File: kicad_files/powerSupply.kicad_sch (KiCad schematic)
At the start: 6 parts, among them U5 TPS61088RHLR

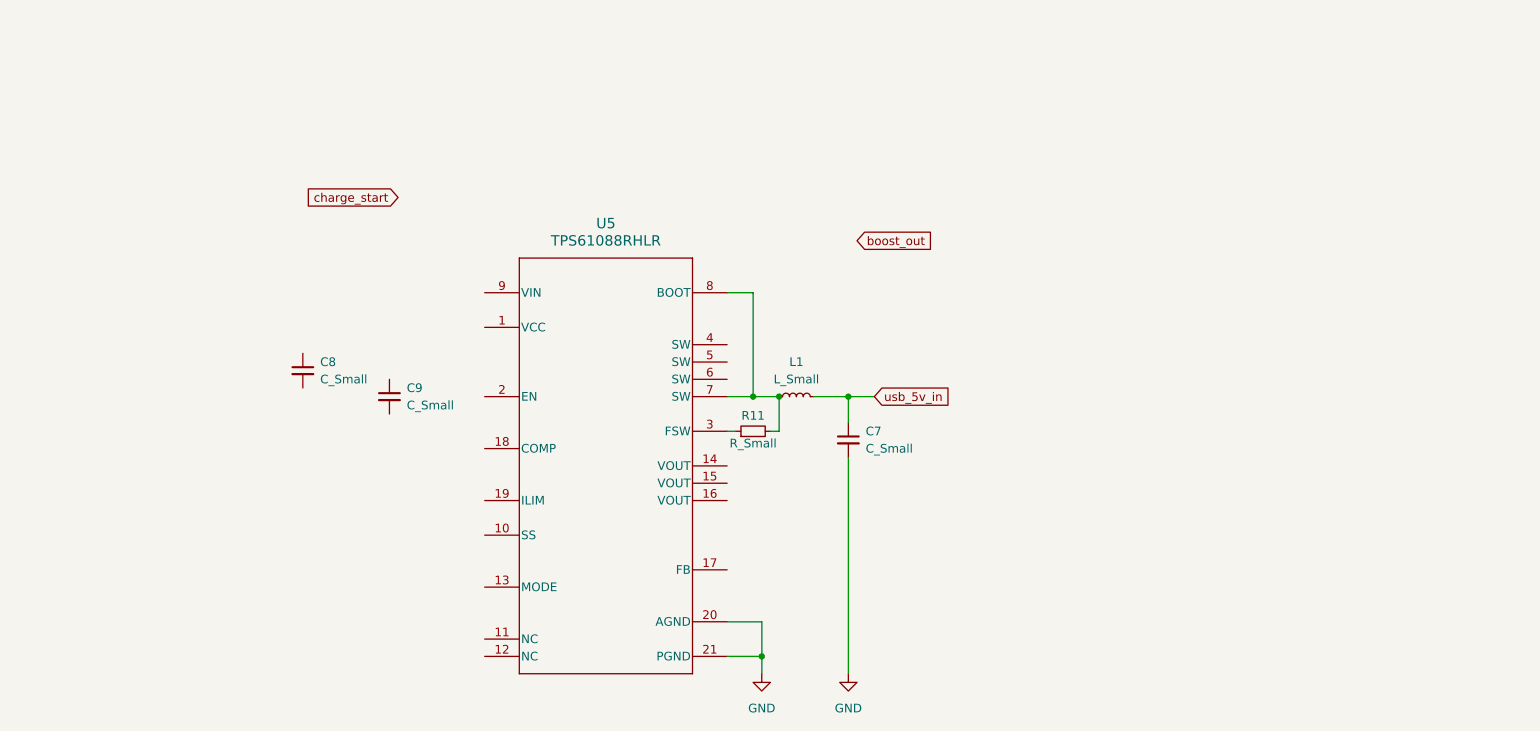
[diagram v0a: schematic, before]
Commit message: finished TI power chip schematic (no values)
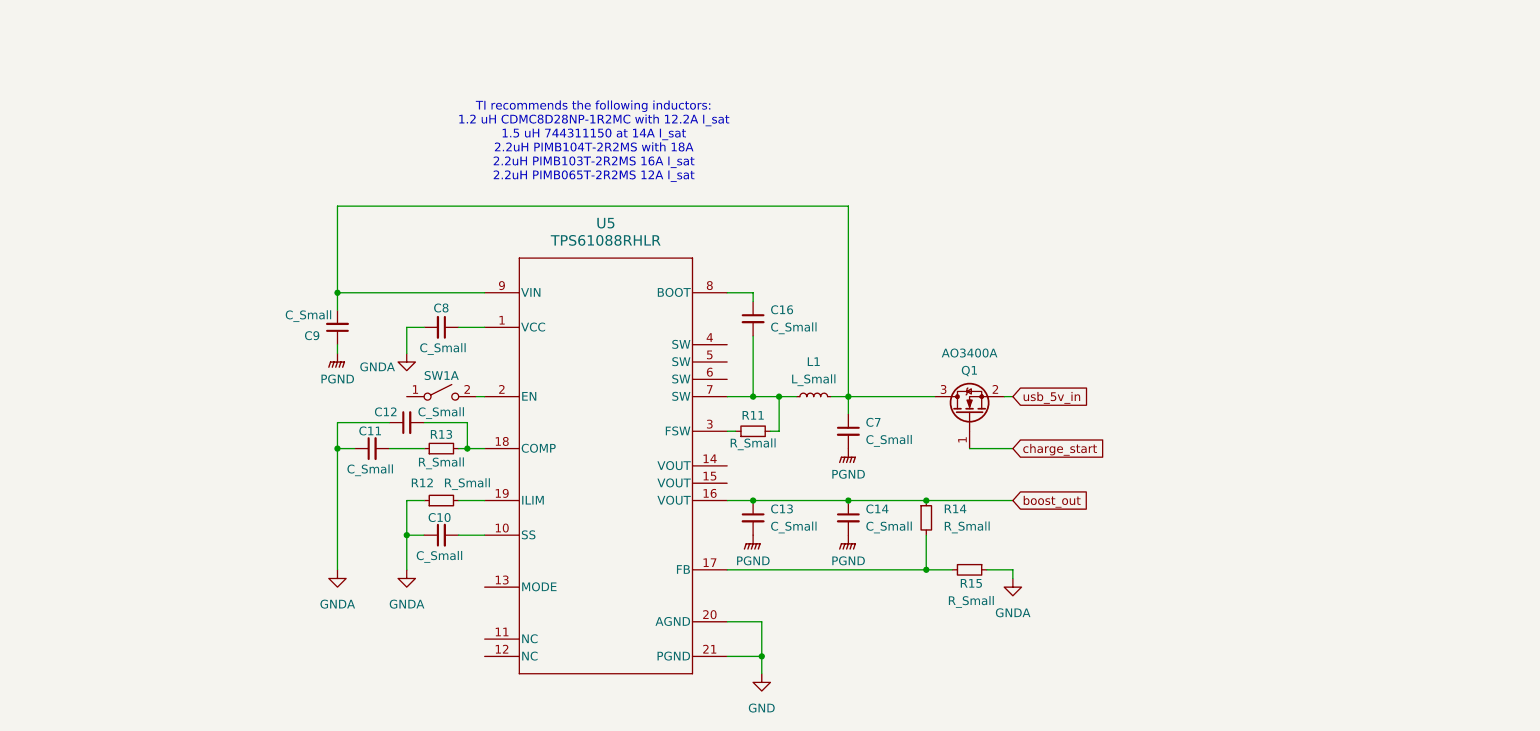
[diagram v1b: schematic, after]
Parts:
- added C10, C11, C12, C13, C14, C16: C_Small, symbol Device:C_Small
- added Q1: AO3400A, Package_TO_SOT_SMD:SOT-23, symbol Transistor_FET:AO3400A
- added R12, R13, R14, R15: R_Small, symbol Device:R_Small
- added SW1: SW_DPST_x2, symbol Switch:SW_DPST_x2
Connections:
- net GND: no longer C7.2
- net boost_out: now also U5.16 (VOUT), C13.1, C14.1, R14.1
- net charge_start: now also Q1.1 (G)
- net usb_5v_in: now also Q1.2 (S); no longer C7.1, L1.2
- net at L1.1, R11.2, U5.7 (SW): now also C16.2; no longer U5.8 (BOOT)
- net PGND: now reaches C9.1
- net PGND: now also C7.2, C13.2, C14.2
- net at C9.2: now also C7.1, L1.2, U5.9 (VIN), Q1.3 (D)
- net at C8.1: now also U5.1 (VCC)
- net GNDA: now reaches C8.2
- net GNDA: now also C10.1, C11.1, C12.1, R12.1, R15.1
- net at U5.10 (SS): now also C10.2
- net at U5.17 (FB): now also R14.2, R15.2
- net at U5.18 (COMP): now also C12.2, R13.2
- net at U5.19 (ILIM): now also R12.2
- net at U5.2 (EN): now also SW1.2 (B)
- new net: C11.2, R13.1
- new net: C16.1, U5.8 (BOOT)
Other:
- note added: "TI recommends the following inductors: 1.2 uH CDMC8D28NP-1R2MC with 12.2A I_sat 1.5 uH 744311150 at 14A I_sat 2.2uH PIMB104T-2R2MS with 18A 2.2uH PIMB103T-2R2MS 16A I_sat 2.2uH PIMB065T-2R2MS 12A I_sat"
- moved on the sheet: C7, C8, C9, L1

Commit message: added symbols for TPS and INA2, sim values for TPS
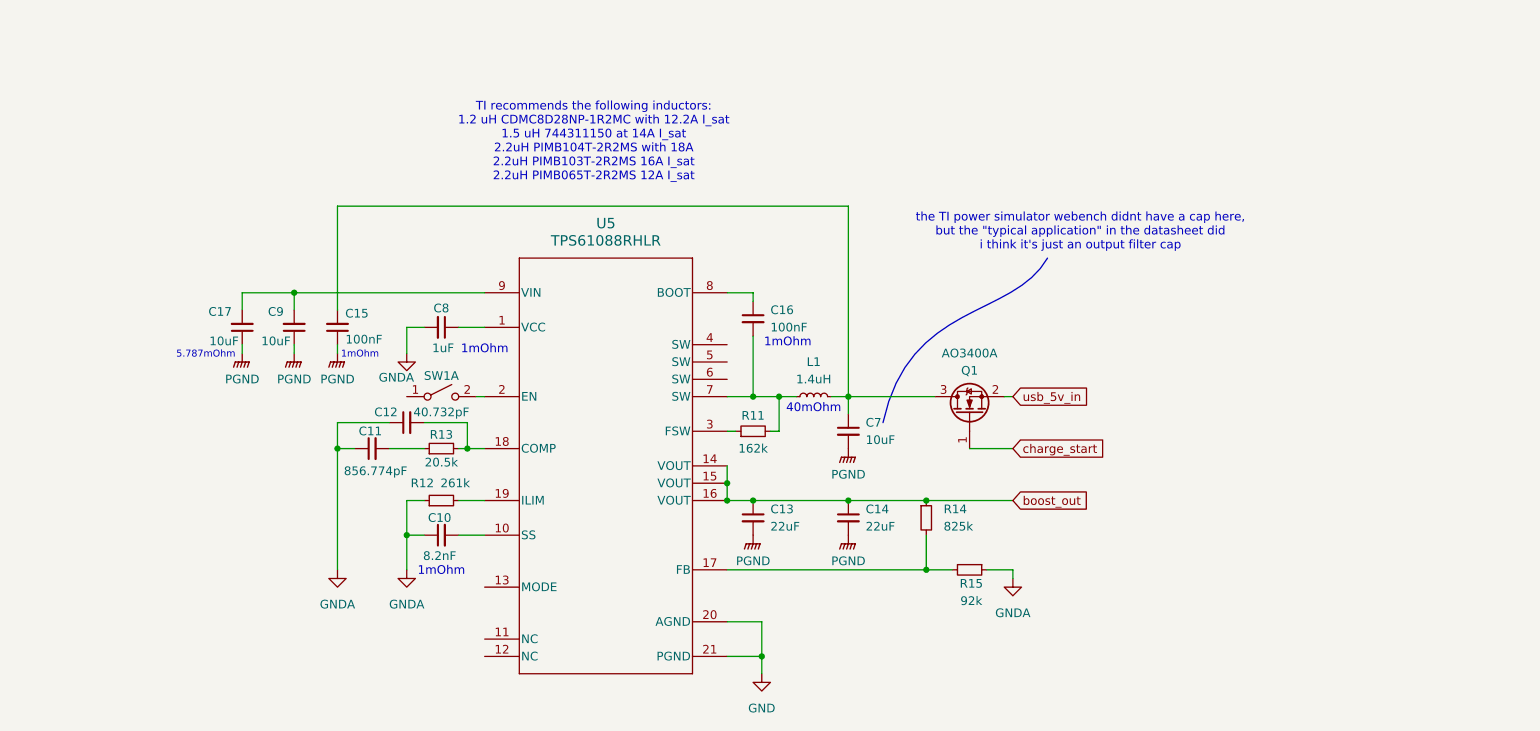
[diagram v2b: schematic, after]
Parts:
- added C15: 100nF, symbol Device:C_Small
- added C17: 10uF, symbol Device:C_Small
- C10: value C_Small -> 8.2nF
- C11: value C_Small -> 856.774pF
- C12: value C_Small -> 40.732pF
- C13, C14: value C_Small -> 22uF
- C16: value C_Small -> 100nF
- C7, C9: value C_Small -> 10uF
- C8: value C_Small -> 1uF
- L1: value L_Small -> 1.4uH
- R11: value R_Small -> 162k
- R12: value R_Small -> 261k
- R13: value R_Small -> 20.5k
- R14: value R_Small -> 825k
- R15: value R_Small -> 92k
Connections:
- net PGND: now also C15.1, C17.1
- net boost_out: now also U5.14 (VOUT), U5.15 (VOUT)
- net at C7.1, L1.2, Q1.3 (D): now also C15.2; no longer C9.2, U5.9 (VIN)
- new net: C17.2, C9.2, U5.9 (VIN)
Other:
- note added: "1mOhm"
- note added: "40mOhm"
- note added: "5.787mOhm"
- note added: "the TI power simulator webench didnt have a cap here, but the "typical application" in the datasheet did i think it's just an output filter cap"
- moved on the sheet: C9

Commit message: more laying out
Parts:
- C10, C11, C12, C13, C14, C15, C16, C17, C7, C8, C9: footprint (none) -> Capacitor_SMD:C_0805_2012Metric_Pad1.18x1.45mm_HandSolder
- L1: footprint (none) -> Inductor_SMD:L_0201_0603Metric
- R11, R12, R13, R14, R15: footprint (none) -> Resistor_SMD:R_0805_2012Metric_Pad1.20x1.40mm_HandSolder
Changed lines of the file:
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@@
 			)
 		)
-		(property "Footprint" ""
+		(property "Footprint" "Capacitor_SMD:C_0805_2012Metric_Pad1.18x1.45mm_HandSolder"
 			(at 127 93.98 0)
 			(hide yes)
@@
 			)
 		)
-		(property "Footprint" ""
+		(property "Footprint" "Capacitor_SMD:C_0805_2012Metric_Pad1.18x1.45mm_HandSolder"
 			(at 172.72 91.44 0)
 			(hide yes)
@@
 			)
 		)
-		(property "Footprint" ""
+		(property "Footprint" "Capacitor_SMD:C_0805_2012Metric_Pad1.18x1.45mm_HandSolder"
 			(at 121.92 77.47 0)
 			(hide yes)
@@
 			)
 		)
-		(property "Footprint" ""
+		(property "Footprint" "Resistor_SMD:R_0805_2012Metric_Pad1.20x1.40mm_HandSolder"
 			(at 204.47 99.06 0)
 			(hide yes)
@@
 			)
 		)
-		(property "Footprint" ""
+		(property "Footprint" "Inductor_SMD:L_0201_0603Metric"
 			(at 181.61 73.66 0)
 			(hide yes)
@@
 			)
 		)
-		(property "Footprint" ""
+		(property "Footprint" "Capacitor_SMD:C_0805_2012Metric_Pad1.18x1.45mm_HandSolder"
 			(at 97.79 63.5 0)
 			(hide yes)
@@
 			)
 		)
-		(property "Footprint" ""
+		(property "Footprint" "Capacitor_SMD:C_0805_2012Metric_Pad1.18x1.45mm_HandSolder"
 			(at 116.84 81.28 0)
 			(hide yes)
@@
 			)
 		)
-		(property "Footprint" ""
+		(property "Footprint" "Capacitor_SMD:C_0805_2012Metric_Pad1.18x1.45mm_HandSolder"
 			(at 105.41 63.5 0)
 			(hide yes)
@@
 			)
 		)
-		(property "Footprint" ""
+		(property "Footprint" "Resistor_SMD:R_0805_2012Metric_Pad1.20x1.40mm_HandSolder"
 			(at 198.12 91.44 0)
 			(hide yes)
@@
 			)
 		)
-		(property "Footprint" ""
+		(property "Footprint" "Resistor_SMD:R_0805_2012Metric_Pad1.20x1.40mm_HandSolder"
 			(at 127 81.28 0)
 			(hide yes)
@@
 			)
 		)
-		(property "Footprint" ""
+		(property "Footprint" "Resistor_SMD:R_0805_2012Metric_Pad1.20x1.40mm_HandSolder"
 			(at 127 88.9 0)
 			(hide yes)
@@
 			)
 		)
-		(property "Footprint" ""
+		(property "Footprint" "Capacitor_SMD:C_0805_2012Metric_Pad1.18x1.45mm_HandSolder"
 			(at 186.69 78.74 0)
 			(hide yes)
@@
 			)
 		)
-		(property "Footprint" ""
+		(property "Footprint" "Capacitor_SMD:C_0805_2012Metric_Pad1.18x1.45mm_HandSolder"
 			(at 127 63.5 0)
 			(hide yes)
@@
 			)
 		)
-		(property "Footprint" ""
+		(property "Footprint" "Capacitor_SMD:C_0805_2012Metric_Pad1.18x1.45mm_HandSolder"
 			(at 172.72 62.23 0)
 			(hide yes)
@@
 			)
 		)
-		(property "Footprint" ""
+		(property "Footprint" "Resistor_SMD:R_0805_2012Metric_Pad1.20x1.40mm_HandSolder"
 			(at 172.72 78.74 0)
 			(hide yes)
@@
 			)
 		)
-		(property "Footprint" ""
+		(property "Footprint" "Capacitor_SMD:C_0805_2012Metric_Pad1.18x1.45mm_HandSolder"
 			(at 111.76 63.5 0)
 			(hide yes)
@@
 			)
 		)
-		(property "Footprint" ""
+		(property "Footprint" "Capacitor_SMD:C_0805_2012Metric_Pad1.18x1.45mm_HandSolder"
 			(at 186.69 91.44 0)
 			(hide yes)

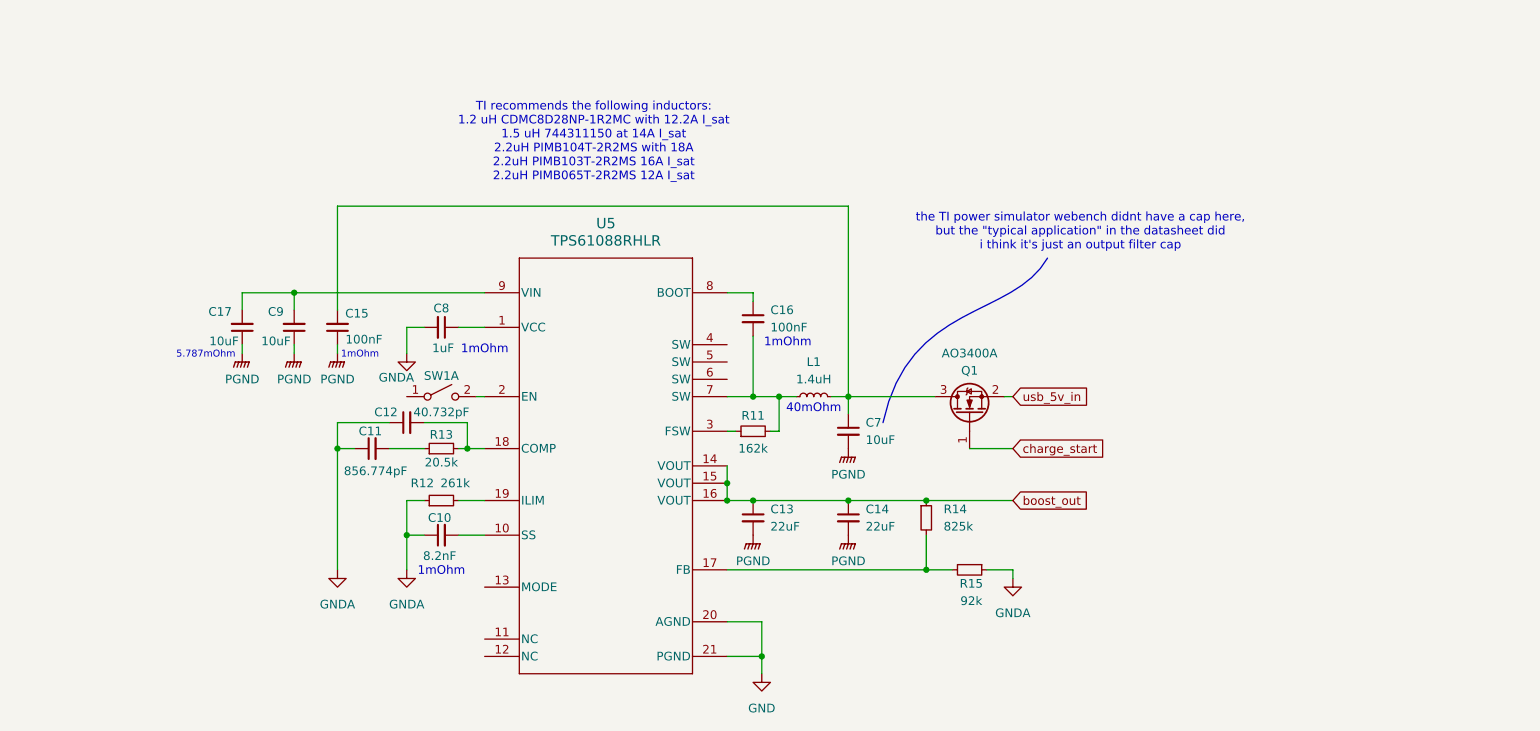
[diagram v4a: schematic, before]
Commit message: added spots for constant current and constant voltage charging stages
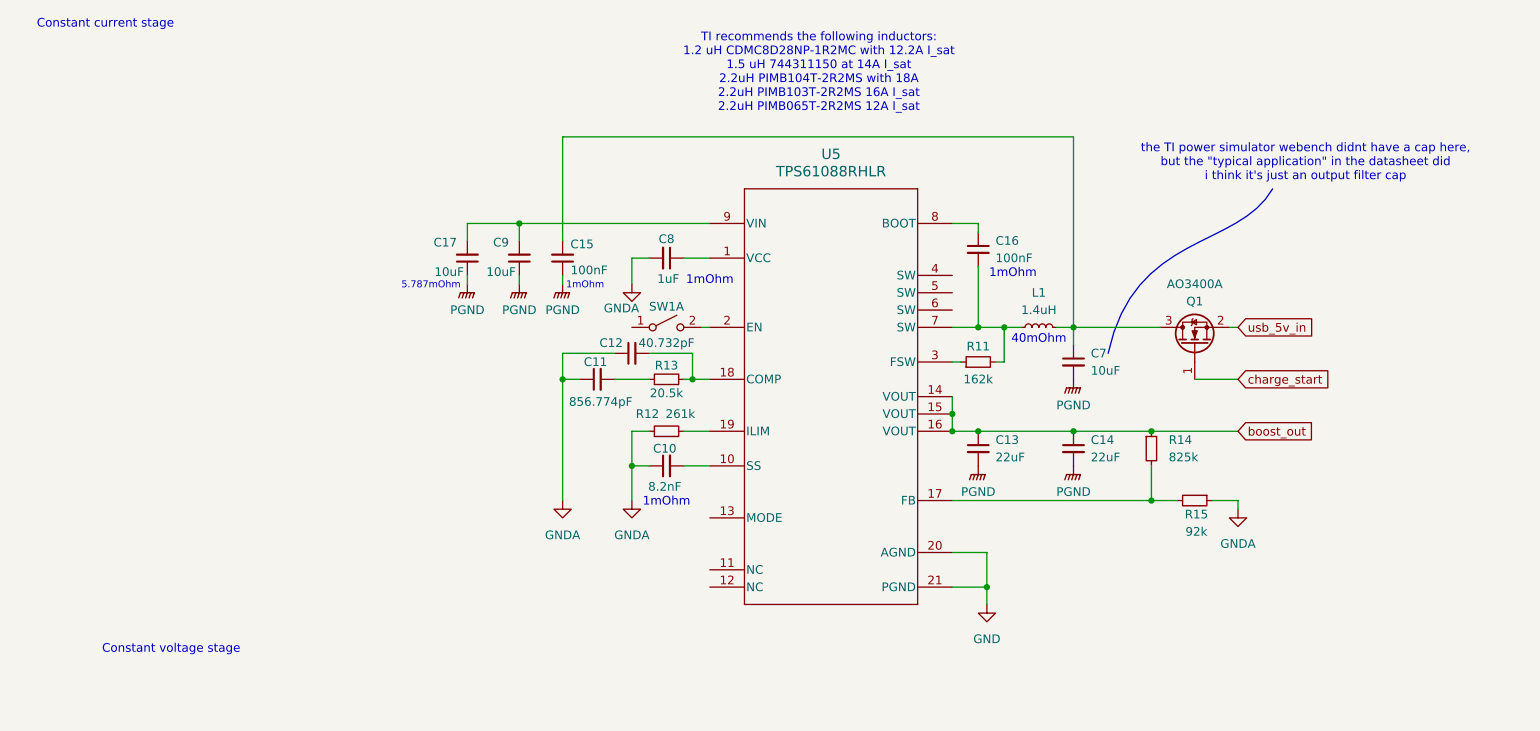
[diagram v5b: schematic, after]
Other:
- note added: "Constant current stage"
- note added: "Constant voltage stage"
- moved on the sheet: C10, C11, C12, C13, C14, C15, C16, C17, C7, C8, C9, L1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
